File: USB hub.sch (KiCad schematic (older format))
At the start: 41 parts, among them IC1 24SN, IC2 FE1.1S, J3 USB_A_SMT_FEMALE, J4 USB_A_SMT_FEMALE, J5 USB_A_SMT_FEMALE, P1 Lily58-cache_CONN_01X04, X1 12MHz

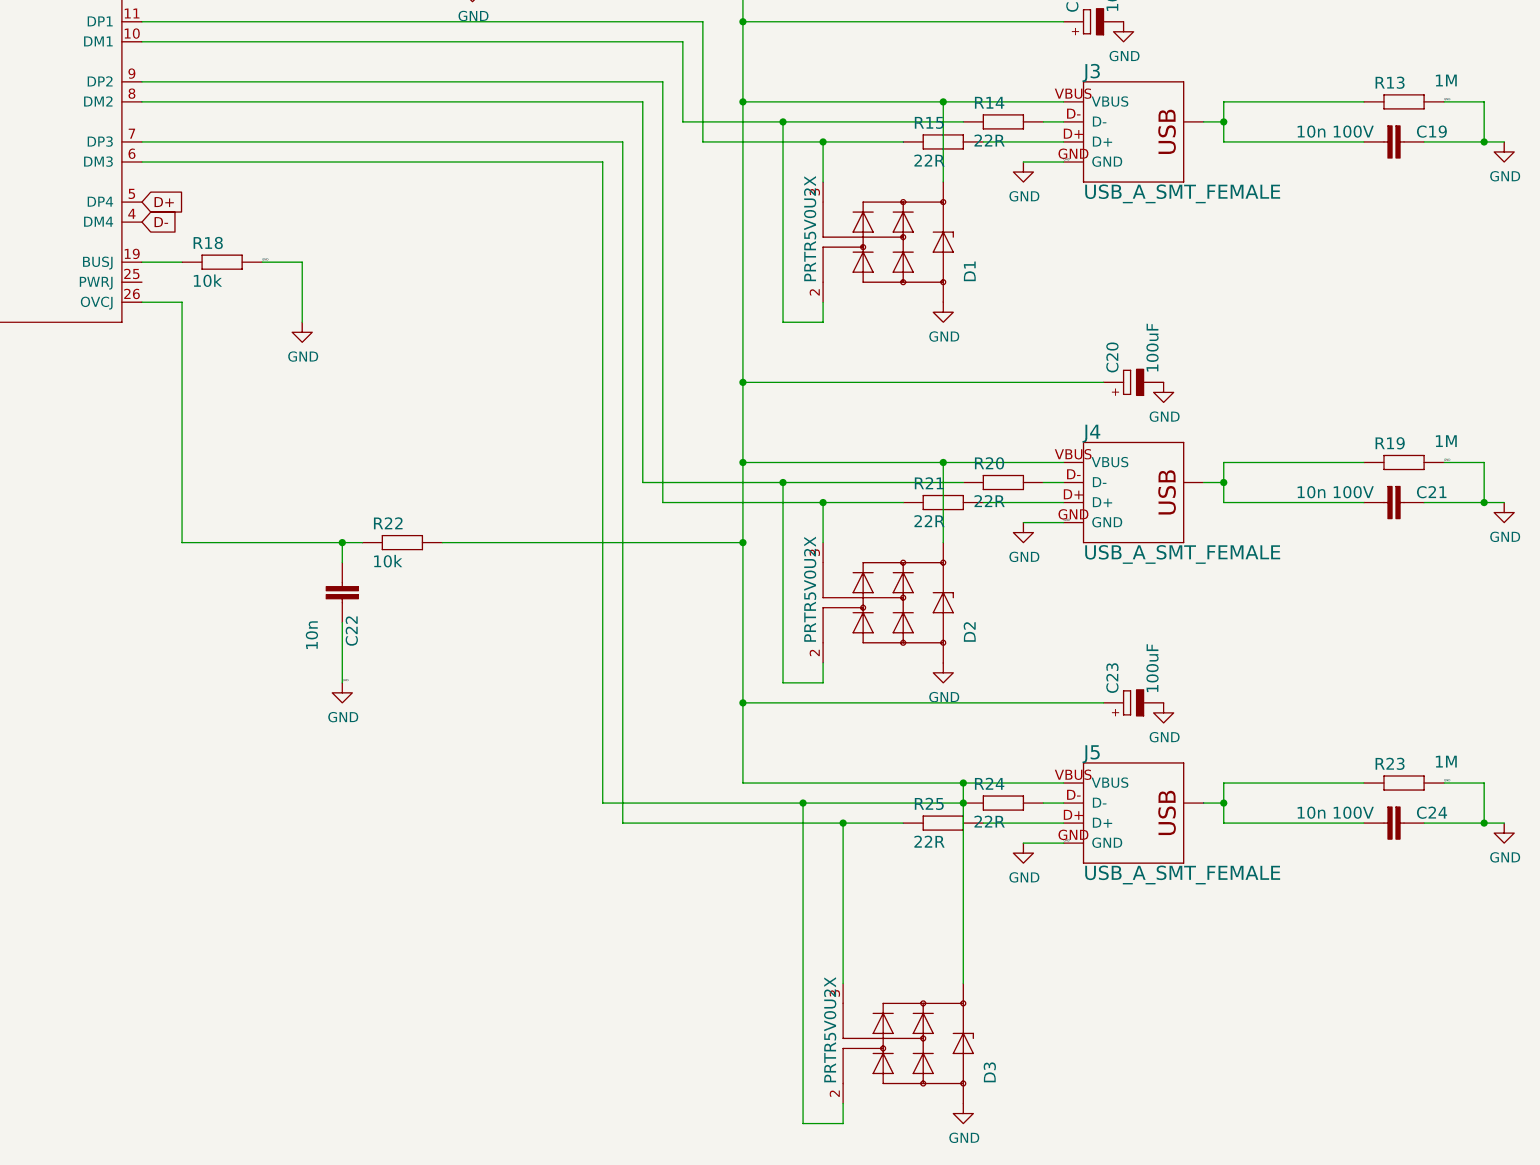
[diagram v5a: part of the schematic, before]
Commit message: removed 1 usb
Removed 1 USB from hub and made rotary bump less pronounced
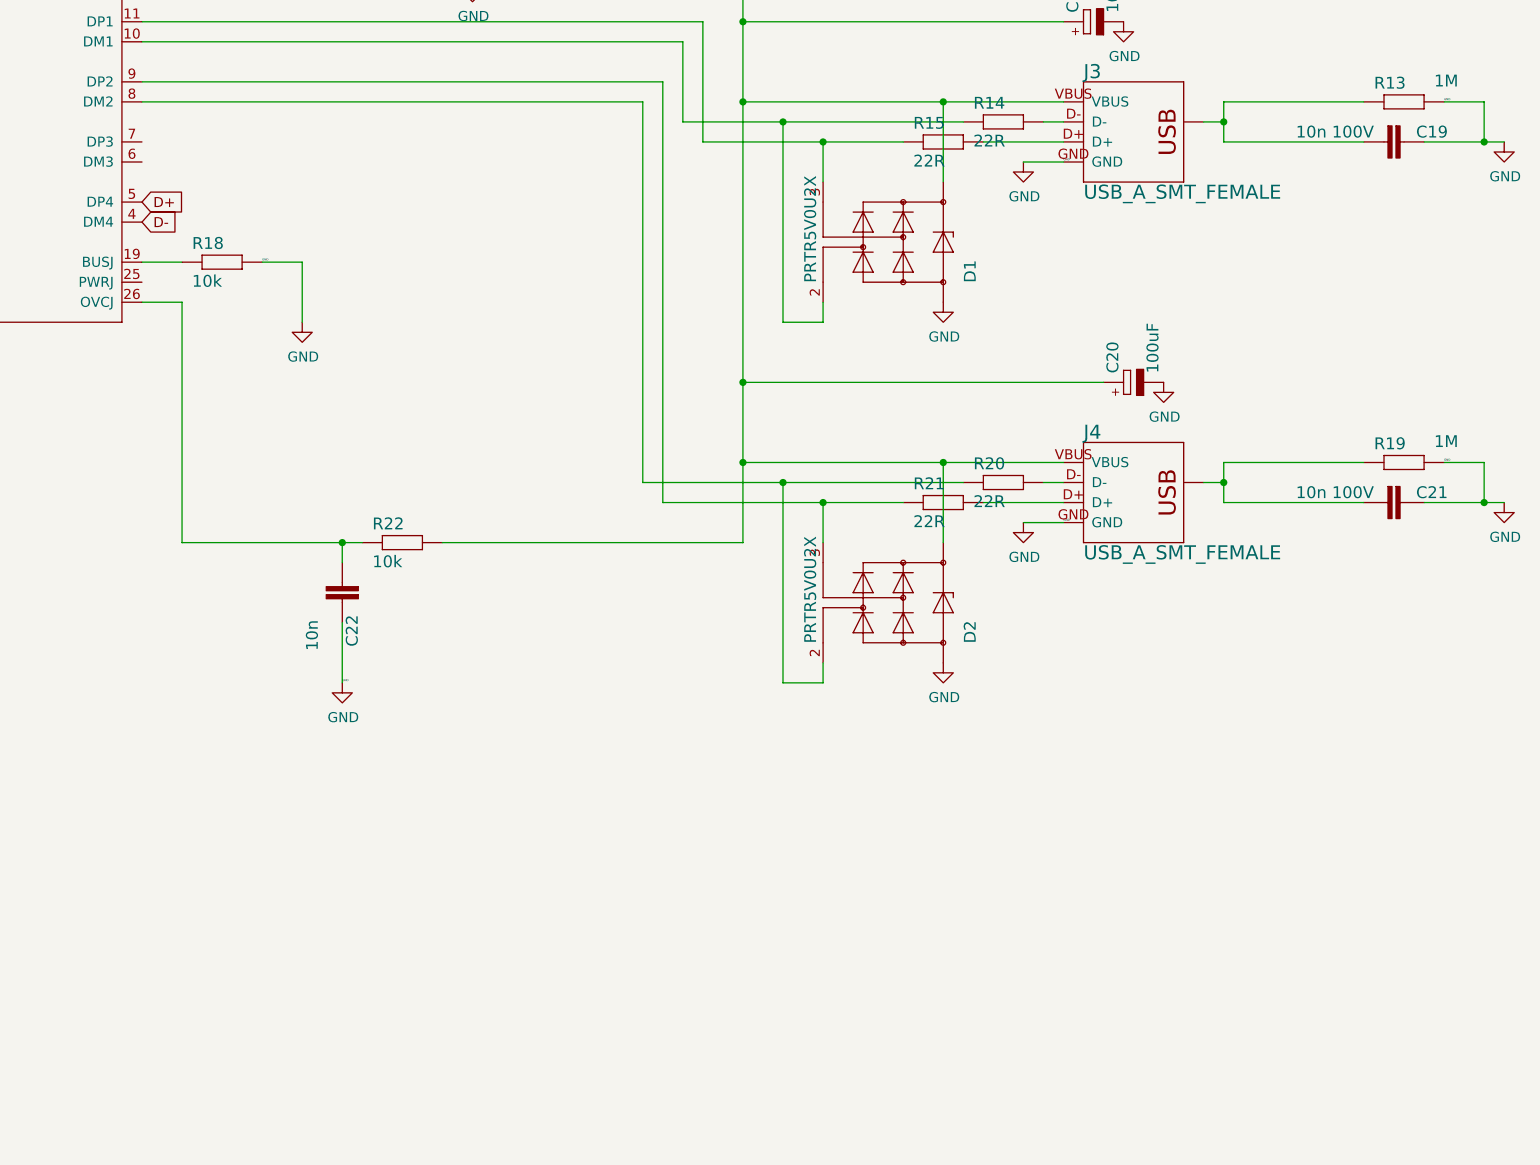
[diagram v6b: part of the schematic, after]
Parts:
- removed C23: 100uF, hub_keyboard:CT3528, symbol hub_keyboard-eagle-import:CPOL-EUCT3528
- removed C24: 10n 100V, Capacitor_SMD:C_0805_2012Metric, symbol hub_keyboard-eagle-import:C-EUC0603
- removed D3: PRTR5V0U2X, hub_keyboard:SOT143, symbol hub_keyboard-eagle-import:PRTR5V0U2X
- removed J5: USB_A_SMT_FEMALE, hub_keyboard:USB-A-S-SILK-FEMALE, symbol hub_keyboard-eagle-import:USB_A_SMT_FEMALE
- removed R23: 1M, 1_Keyboard Footprints:R_0603, symbol hub_keyboard-eagle-import:R-EU_R0603
- removed R24, R25: 22R, 1_Keyboard Footprints:R_0603, symbol hub_keyboard-eagle-import:R-EU_R0603
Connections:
- net at C12.+, C20.+, D1.4 (VCC)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: no longer IC2.6 (DM3)
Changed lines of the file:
@@
-$EndComp
-$Comp
-L power:GND #PWR0146
-U 1 1 5FC90B96
-P 10750 8350
-F 0 "#PWR0146" H 10750 8100 50  0001 C CNN
-F 1 "GND" H 10755 8177 50  0000 C CNN
-F 2 "" H 10750 8350 50  0001 C CNN
-F 3 "" H 10750 8350 50  0001 C CNN
-	1    10750 8350
-	1    0    0    -1
 $EndComp
 $Comp
@@
 $EndComp
 $Comp
-L power:GND #PWR0143
-U 1 1 5FC6DDBC
-P 11450 7650
-F 0 "#PWR0143" H 11450 7400 50  0001 C CNN
-F 1 "GND" H 11455 7477 50  0000 C CNN
-F 2 "" H 11450 7650 50  0001 C CNN
-F 3 "" H 11450 7650 50  0001 C CNN
-	1    11450 7650
-	1    0    0    -1
-$EndComp
-$Comp
-L power:GND #PWR0142
-U 1 1 5FC62285
-P 13150 8250
-F 0 "#PWR0142" H 13150 8000 50  0001 C CNN
-F 1 "GND" H 13155 8077 50  0000 C CNN
-F 2 "" H 13150 8250 50  0001 C CNN
-F 3 "" H 13150 8250 50  0001 C CNN
-	1    13150 8250
-	1    0    0    -1
-$EndComp
-$Comp
 L power:GND #PWR0141
 U 1 1 5FC61D84
@@
 	1    0    0    -1
 $EndComp
-$Comp
-L power:GND #PWR0116
-U 1 1 5FB691D5
-P 10450 9650
-F 0 "#PWR0116" H 10450 9400 50  0001 C CNN
-F 1 "GND" H 10455 9477 50  0000 C CNN
-F 2 "" H 10450 9650 50  0001 C CNN
-F 3 "" H 10450 9650 50  0001 C CNN
-	1    10450 9650
-	1    0    0    -1
-$EndComp
 Text GLabel 6350 5250 2    50   Input ~ 0
 D-
 Text GLabel 6350 5150 2    50   Input ~ 0
 D+
-$Comp
-L hub_keyboard-eagle-import:R-EU_R0603 R?
-U 1 1 84C3B2F5
-P 10350 8250
-AR Path="/84C3B2F5" Ref="R?"  Part="1"
-AR Path="/5EFCC321/84C3B2F5" Ref="R?"  Part="1"
-AR Path="/5F06AC00/84C3B2F5" Ref="R25"  Part="1"
-F 0 "R25" H 10200 8309 59  0000 L BNN
-F 1 "22R" H 10200 8120 59  0000 L BNN
-F 2 "1_Keyboard Footprints:R_0603" H 10350 8250 50  0001 C CNN
-F 3 "" H 10350 8250 50  0001 C CNN
-F 4 "C23345" H 10350 8250 59  0001 L BNN "LCSC"
-	1    10350 8250
-	1    0    0    -1
-$EndComp
-$Comp
-L hub_keyboard-eagle-import:R-EU_R0603 R?
-U 1 1 D5EFCBE0
-P 10650 8150
-AR Path="/D5EFCBE0" Ref="R?"  Part="1"
-AR Path="/5EFCC321/D5EFCBE0" Ref="R?"  Part="1"
-AR Path="/5F06AC00/D5EFCBE0" Ref="R24"  Part="1"
-F 0 "R24" H 10500 8209 59  0000 L BNN
-F 1 "22R" H 10500 8020 59  0000 L BNN
-F 2 "1_Keyboard Footprints:R_0603" H 10650 8150 50  0001 C CNN
-F 3 "" H 10650 8150 50  0001 C CNN
-F 4 "C23345" H 10650 8150 59  0001 L BNN "LCSC"
-	1    10650 8150
-	1    0    0    -1
-$EndComp
 $Comp
 L hub_keyboard-eagle-import:R-EU_R0603 R?
@@
 	1    10650 4750
 	1    0    0    -1
-$EndComp
-$Comp
-L hub_keyboard-eagle-import:PRTR5V0U2X D?
-U 1 1 72C1871A
-P 10150 9350
-AR Path="/72C1871A" Ref="D?"  Part="1"
-AR Path="/5EFCC321/72C1871A" Ref="D?"  Part="1"
-AR Path="/5F06AC00/72C1871A" Ref="D3"  Part="1"
-F 0 "D3" H 9948 9750 59  0000 L BNN
-F 1 "PRTR5V0U2X" H 9948 8953 59  0000 L BNN
-F 2 "hub_keyboard:SOT143" H 10150 9350 50  0001 C CNN
-F 3 "" H 10150 9350 50  0001 C CNN
-F 4 "1727-3884-1-ND" H 10150 9350 59  0001 L BNN "DIGIKEY"
-F 5 "TRUE" H 10150 9350 59  0001 L BNN "EXTENDED"
-F 6 "1524157" H 10150 9350 59  0001 L BNN "FARNELL"
-F 7 "C384891" H 10150 9350 59  0001 L BNN "LCSC"
-	1    10150 9350
-	0    1    -1   0
 $EndComp
 $Comp
@@
 $Comp
 L hub_keyboard-eagle-import:CPOL-EUCT3528 C?
-U 1 1 CD35B308
-P 11250 7650
-AR Path="/CD35B308" Ref="C?"  Part="1"
-AR Path="/5EFCC321/CD35B308" Ref="C?"  Part="1"
-AR Path="/5F06AC00/CD35B308" Ref="C23"  Part="1"
-F 0 "C23" H 11295 7669 59  0000 L BNN
-F 1 "100uF" H 11295 7469 59  0000 L BNN
-F 2 "hub_keyboard:CT3528" H 11250 7650 50  0001 C CNN
-F 3 "" H 11250 7650 50  0001 C CNN
-F 4 "C16133" H 11250 7650 59  0001 L BNN "LCSC"
-	1    11250 7650
-	0    -1   -1   0
-$EndComp
-$Comp
-L hub_keyboard-eagle-import:CPOL-EUCT3528 C?
 U 1 1 DF433A60
 P 11250 6050
@@
 	1    2950 4450
 	-1   0    0    1
-$EndComp
-$Comp
-L hub_keyboard-eagle-import:R-EU_R0603 R?
-U 1 1 99B5315F
-P 12650 8050
-AR Path="/99B5315F" Ref="R?"  Part="1"
-AR Path="/5EFCC321/99B5315F" Ref="R?"  Part="1"
-AR Path="/5F06AC00/99B5315F" Ref="R23"  Part="1"
-F 0 "R23" H 12500 8109 59  0000 L BNN
-F 1 "1M" H 12800 8120 59  0000 L BNN
-F 2 "1_Keyboard Footprints:R_0603" H 12650 8050 50  0001 C CNN
-F 3 "" H 12650 8050 50  0001 C CNN
-F 4 "C22935" H 12650 8050 59  0001 L BNN "LCSC"
-	1    12650 8050
-	1    0    0    -1
-$EndComp
-$Comp
-L hub_keyboard-eagle-import:C-EUC0603 C?
-U 1 1 3C437C10
-P 12650 8250
-AR Path="/3C437C10" Ref="C?"  Part="1"
-AR Path="/5EFCC321/3C437C10" Ref="C?"  Part="1"
-AR Path="/5F06AC00/3C437C10" Ref="C24"  Part="1"
-F 0 "C24" V 12635 8310 59  0000 L BNN
-F 1 "10n 100V" V 12635 7710 59  0000 L BNN
-F 2 "Capacitor_SMD:C_0805_2012Metric" H 12650 8250 50  0001 C CNN
-F 3 "" H 12650 8250 50  0001 C CNN
-F 4 "TRUE" H 12650 8250 59  0001 L BNN "EXTENDED"
-F 5 "C84709" H 12650 8250 59  0001 L BNN "LCSC"
-	1    12650 8250
-	0    1    1    0
 $EndComp
 $Comp
@@
 $Comp
 L hub_keyboard-eagle-import:USB_A_SMT_FEMALE J?
-U 1 1 92202B0B
-P 11250 8250
-AR Path="/92202B0B" Ref="J?"  Part="1"
-AR Path="/5EFCC321/92202B0B" Ref="J?"  Part="1"
-AR Path="/5F06AC00/92202B0B" Ref="J5"  Part="1"
-F 0 "J5" H 11050 8560 70  0000 L BNN
-F 1 "USB_A_SMT_FEMALE" H 11050 8040 70  0000 L TNN
-F 2 "hub_keyboard:USB-A-S-SILK-FEMALE" H 11250 8250 50  0001 C CNN
-F 3 "" H 11250 8250 50  0001 C CNN
-F 4 "609-4946-1-ND" H 11250 8250 70  0001 L BNN "DIGIKEY"
-	1    11250 8250
-	1    0    0    -1
-$EndComp
-$Comp
-L hub_keyboard-eagle-import:USB_A_SMT_FEMALE J?
 U 1 1 F1780596
 P 11250 6650
@@
 $EndComp
 Wire Wire Line
-	10950 8250 10550 8250
-Wire Wire Line
-	10950 8150 10850 8150
-Wire Wire Line
 	10550 6650 10950 6650
 Wire Wire Line
@@
 Wire Wire Line
 	7450 6850 7350 6850
-Connection ~ 10450 8050
 Connection ~ 10350 6450
 Connection ~ 10350 4650
-Connection ~ 9350 6850
 Connection ~ 9350 4250
-Connection ~ 9350 7650
 Connection ~ 9350 6450
 Connection ~ 9350 6050
 Connection ~ 9350 4650
 Wire Wire Line
-	10450 9050 10450 8150
-Wire Wire Line
 	10350 6850 10350 6450
 Wire Wire Line
@@
 	10950 6450 10350 6450
 Wire Wire Line
-	10450 8050 9350 8050
-Wire Wire Line
-	10950 8050 10450 8050
-Wire Wire Line
-	9350 6850 9350 7650
-Wire Wire Line
 	9350 6450 9350 6850
-Wire Wire Line
-	9350 7650 9350 8050
-Wire Wire Line
-	11150 7650 9350 7650
 Wire Wire Line
 	9350 4650 9350 6050
@@
 Wire Wire Line
 	4950 4050 4650 4050
-Connection ~ 11750 8150
-Wire Wire Line
-	11750 8250 11750 8150
-Wire Wire Line
-	12450 8250 11750 8250
-Wire Wire Line
-	11750 8150 11650 8150
-Wire Wire Line
-	11750 8050 11750 8150
-Wire Wire Line
-	12450 8050 11750 8050
 Connection ~ 11750 6550
 Wire Wire Line
@@
 Wire Wire Line
 	4950 5650 4850 5650
-Text Label 10950 8350 0    10   ~ 0
-GND
-Wire Wire Line
-	10950 8350 10750 8350
 Text Label 10950 6750 0    10   ~ 0
 GND
@@
 Wire Wire Line
 	8200 4050 8000 4050
-Text Label 12850 8050 0    10   ~ 0
-GND
-Connection ~ 13050 8250
-Wire Wire Line
-	13050 8250 13150 8250
-Wire Wire Line
-	13050 8250 12750 8250
-Wire Wire Line
-	13050 8050 13050 8250
-Wire Wire Line
-	12850 8050 13050 8050
 Text Label 12850 6450 0    10   ~ 0
 GND
@@
 Wire Wire Line
 	12850 4650 13050 4650
-Connection ~ 9650 8150
-Wire Wire Line
-	10450 8150 9650 8150
-Wire Wire Line
-	9650 9750 9650 8150
-Wire Wire Line
-	9850 9750 9650 9750
-Wire Wire Line
-	9850 9650 9850 9750
-Wire Wire Line
-	8650 4950 6350 4950
-Wire Wire Line
-	8650 8150 8650 4950
-Wire Wire Line
-	9650 8150 8650 8150
-Connection ~ 9850 8250
-Wire Wire Line
-	10150 8250 9850 8250
-Wire Wire Line
-	9850 9050 9850 8250
-Wire Wire Line
-	8750 4850 6350 4850
-Wire Wire Line
-	8750 8250 8750 4850
-Wire Wire Line
-	9850 8250 8750 8250
 Connection ~ 9750 6650
 Wire Wire Line
@@
 Wire Wire Line
 	9550 4750 9050 4750
-Connection ~ 10450 8150
-Wire Wire Line
-	10450 8150 10450 8050
 $EndSCHEMATC

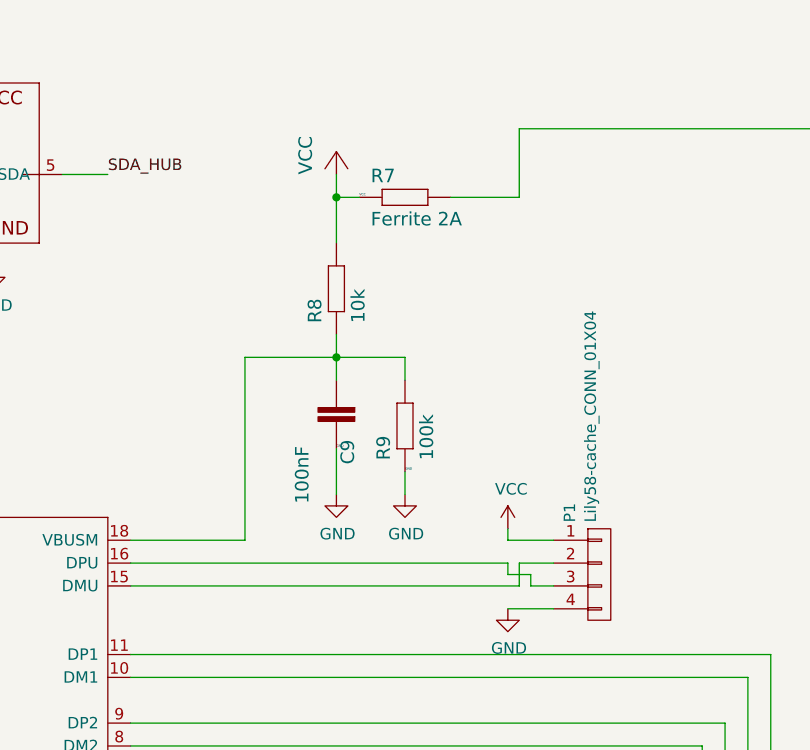
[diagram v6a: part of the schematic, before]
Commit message: route hub
routed usb hub
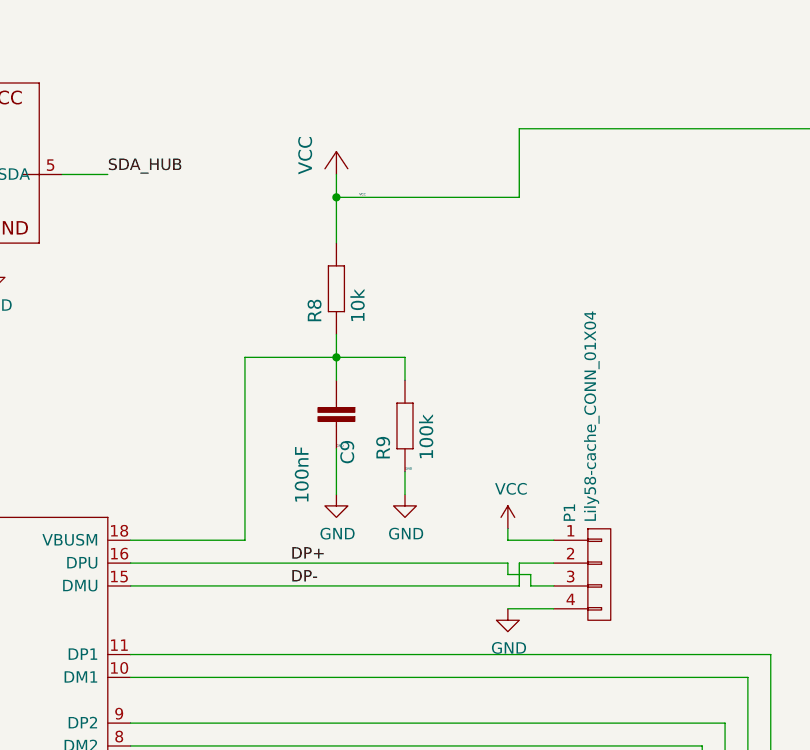
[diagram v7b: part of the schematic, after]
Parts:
- removed R7: Ferrite 2A, hub_keyboard:R0805, symbol hub_keyboard-eagle-import:R-EU_R0805
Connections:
- net VCC: now also C12.+, C20.+, D1.4 (VCC), D2.4 (VCC), J3.VBUS, J4.VBUS, R22.2
- net DP-: now reaches IC2.15 (DMU), P1.2 (P2)
- net DP+: now reaches IC2.16 (DPU), P1.3 (P3)
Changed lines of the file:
@@
 	1    0    0    -1
 $EndComp
-Text GLabel 6350 5250 2    50   Input ~ 0
-D-
-Text GLabel 6350 5150 2    50   Input ~ 0
-D+
 $Comp
 L hub_keyboard-eagle-import:R-EU_R0603 R?
@@
 $EndComp
 $Comp
-L hub_keyboard-eagle-import:R-EU_R0805 R?
-U 1 1 0CE4963D
-P 7550 2250
-AR Path="/0CE4963D" Ref="R?"  Part="1"
-AR Path="/5EFCC321/0CE4963D" Ref="R?"  Part="1"
-AR Path="/5F06AC00/0CE4963D" Ref="R7"  Part="1"
-F 0 "R7" H 7400 2309 59  0000 L BNN
-F 1 "Ferrite 2A" H 7400 2120 59  0000 L BNN
-F 2 "hub_keyboard:R0805" H 7550 2250 50  0001 C CNN
-F 3 "" H 7550 2250 50  0001 C CNN
-F 4 "TRUE" H 7550 2250 59  0001 L BNN "EXTENDED"
-F 5 "C44361" H 7550 2250 59  0001 L BNN "LCSC"
-	1    7550 2250
-	1    0    0    -1
-$EndComp
-$Comp
 L hub_keyboard-eagle-import:R-EU_R0603 R?
 U 1 1 0C3AE8E0
@@
 Wire Wire Line
 	9350 1950 8050 1950
-Wire Wire Line
-	8050 2250 7750 2250
 Connection ~ 7350 6850
 Wire Wire Line
@@
 Wire Wire Line
 	7250 2150 7250 2250
-Wire Wire Line
-	7350 2250 7250 2250
 Text Label 3650 4650 0    10   ~ 0
 GND
@@
 Wire Wire Line
 	9550 4750 9050 4750
+Wire Wire Line
+	7250 2250 8050 2250
+Text GLabel 6350 5150 2    50   Input ~ 0
+D+
+Text GLabel 6350 5250 2    50   Input ~ 0
+D-
+Text Label 7050 3850 0    50   ~ 0
+DP+
+Text Label 7050 3950 0    50   ~ 0
+DP-
 $EndSCHEMATC

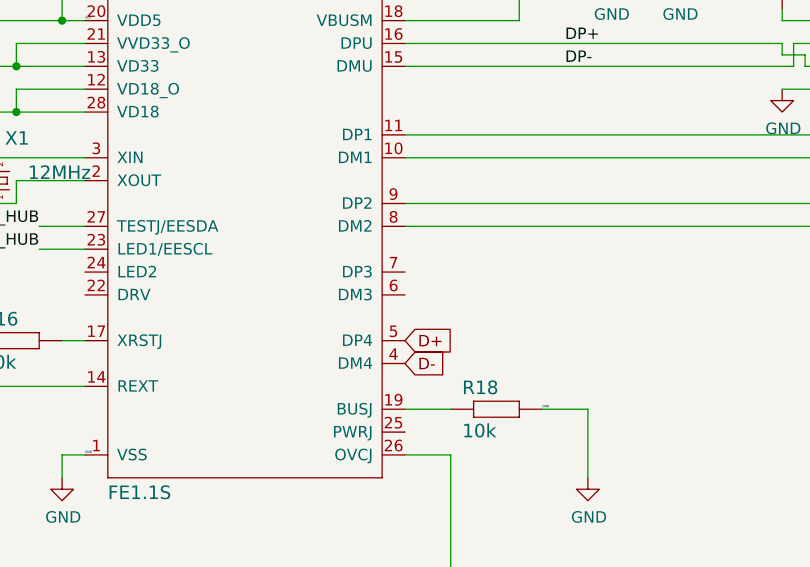
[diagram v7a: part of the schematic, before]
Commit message: add ground plane
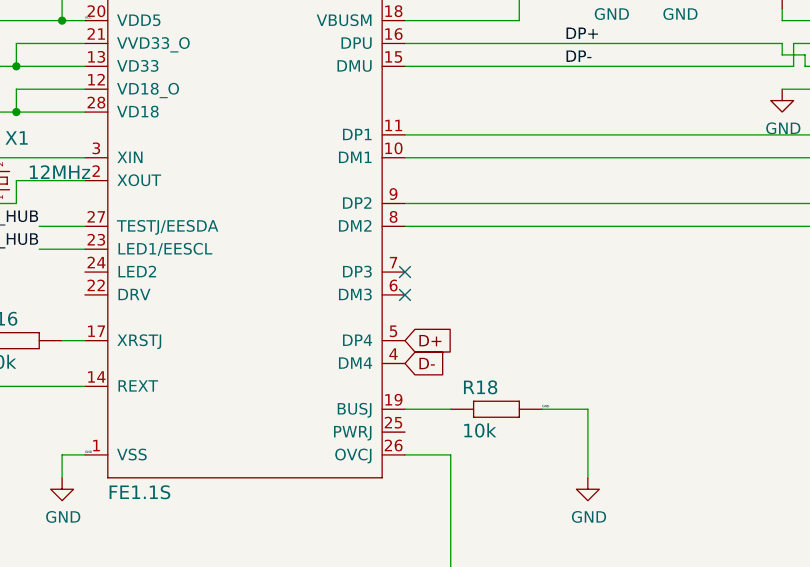
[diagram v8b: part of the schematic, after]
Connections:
- no-connect marks 0 -> 2
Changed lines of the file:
@@
 Text Label 7050 3950 0    50   ~ 0
 DP-
+NoConn ~ 6350 4850
+NoConn ~ 6350 4950
 $EndSCHEMATC
